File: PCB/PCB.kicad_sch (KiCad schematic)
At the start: 21 parts, among them J1 Conn_01x06_Female, U13 74HC165, U16 74HC165

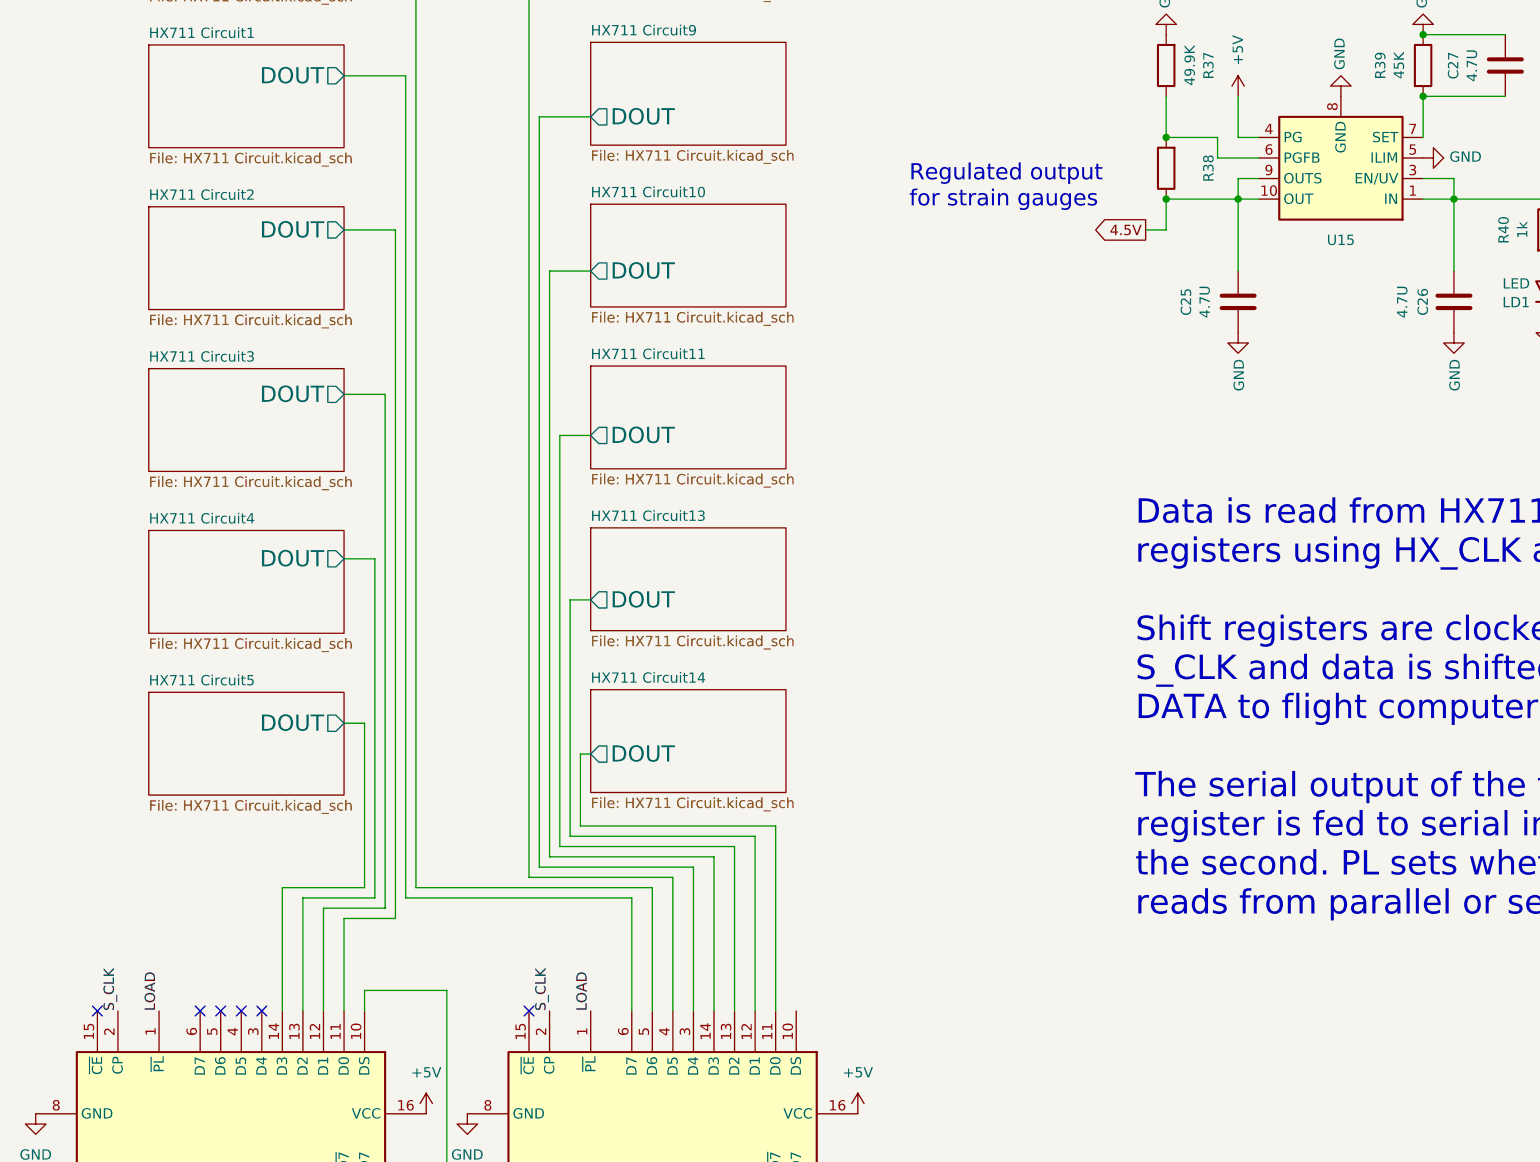
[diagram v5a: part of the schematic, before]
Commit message: Add second decoupling cap to HXs
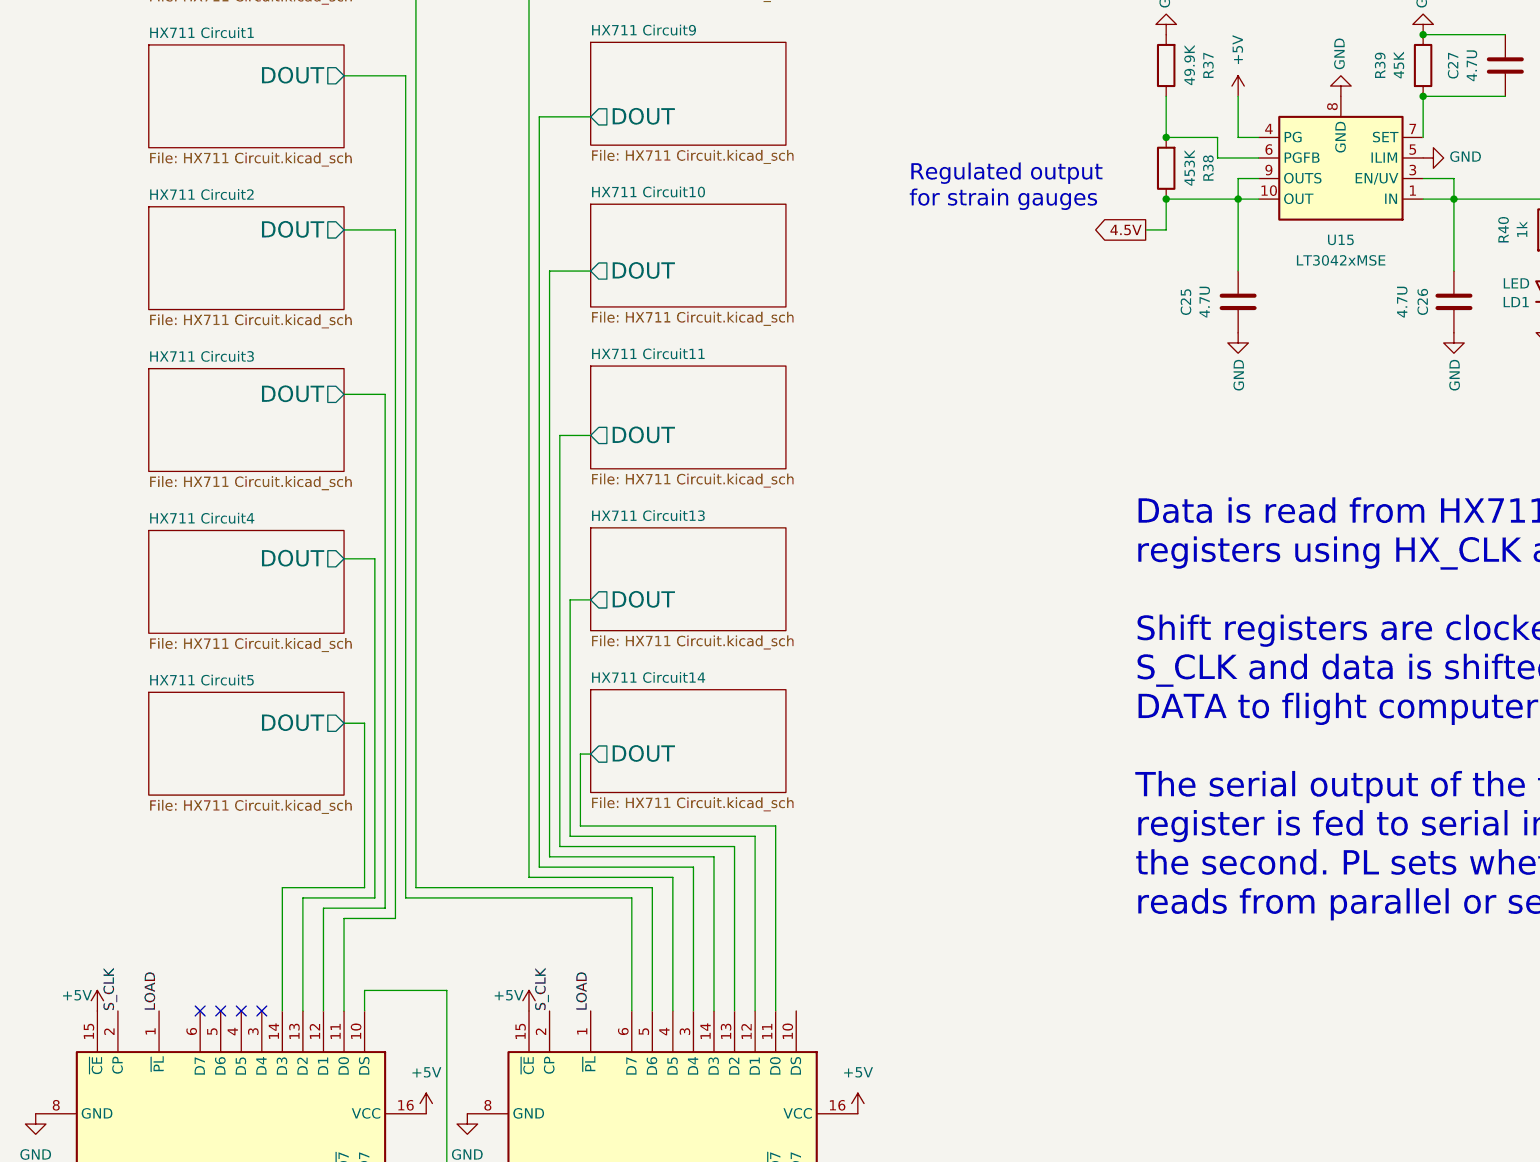
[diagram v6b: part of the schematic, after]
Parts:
- R38: value (none) -> 453K; footprint (none) -> Resistor_SMD:R_0805_2012Metric_Pad1.20x1.40mm_HandSolder
- U15: value (none) -> LT3042xMSE; footprint (none) -> Package_SO:MSOP-10-1EP_3x3mm_P0.5mm_EP1.68x1.88mm
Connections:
- net +5V: now also U13.15 (~{CE}), U16.15 (~{CE})
- no-connect marks 8 -> 6
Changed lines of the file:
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@@
   (no_connect (at 45.72 165.1))
   (no_connect (at 40.64 165.1))
-  (no_connect (at 81.28 165.1))
   (no_connect (at 58.42 190.5))
   (no_connect (at 111.76 190.5))
   (no_connect (at 48.26 165.1))
-  (no_connect (at 27.94 165.1))
   (no_connect (at 43.18 165.1))
   (wire (pts (xy 64.77 68.58) (xy 64.77 153.67))
@@
     (in_bom yes) (on_board yes)
     (property "Reference" "R38" (id 0) (at 165.2778 60.96 90))
-    (property "Value" "" (id 1) (at 162.9664 60.96 90))
-    (property "Footprint" "" (id 2) (at 161.798 60.96 90)
+    (property "Value" "453K" (id 1) (at 162.9664 60.96 90))
+    (property "Footprint" "Resistor_SMD:R_0805_2012Metric_Pad1.20x1.40mm_HandSolder" (id 2) (at 161.798 60.96 90)
       (effects (font (size 1.27 1.27)) hide)
     )
@@
     (in_bom yes) (on_board yes) (fields_autoplaced)
     (property "Reference" "U15" (id 0) (at 181.61 69.85 0))
-    (property "Value" "" (id 1) (at 181.61 72.39 0))
-    (property "Footprint" "" (id 2) (at 181.61 70.485 0)
+    (property "Value" "LT3042xMSE" (id 1) (at 181.61 72.39 0))
+    (property "Footprint" "Package_SO:MSOP-10-1EP_3x3mm_P0.5mm_EP1.68x1.88mm" (id 2) (at 181.61 70.485 0)
       (effects (font (size 1.27 1.27)) hide)
     )
@@
     )
   )
+  (symbol (lib_id "power:+5V") (at 27.94 165.1 0) (unit 1)
+    (in_bom yes) (on_board yes)
+    (property "Reference" "#PWR?" (id 0) (at 27.94 168.91 0)
+      (effects (font (size 1.27 1.27)) hide)
+    )
+    (property "Value" "+5V" (id 1) (at 25.4 163.195 0))
+    (property "Footprint" "" (id 2) (at 27.94 165.1 0)
+      (effects (font (size 1.27 1.27)) hide)
+    )
+    (property "Datasheet" "" (id 3) (at 27.94 165.1 0)
+      (effects (font (size 1.27 1.27)) hide)
+    )
+    (pin "1")
+  )
   (symbol (lib_id "Mechanical:MountingHole") (at 255.27 73.66 180) (unit 1)
     (in_bom yes) (on_board yes)
@@
       (effects (font (size 1.27 1.27)) hide)
     )
+  )
+  (symbol (lib_id "power:+5V") (at 81.28 165.1 0) (unit 1)
+    (in_bom yes) (on_board yes)
+    (property "Reference" "#PWR?" (id 0) (at 81.28 168.91 0)
+      (effects (font (size 1.27 1.27)) hide)
+    )
+    (property "Value" "+5V" (id 1) (at 78.74 163.195 0))
+    (property "Footprint" "" (id 2) (at 81.28 165.1 0)
+      (effects (font (size 1.27 1.27)) hide)
+    )
+    (property "Datasheet" "" (id 3) (at 81.28 165.1 0)
+      (effects (font (size 1.27 1.27)) hide)
+    )
+    (pin "1")
   )
   (symbol (lib_id "74xx:74HC165") (at 99.06 177.8 270) (unit 1)
@@
       (reference "#PWR0176") (unit 1) (value "GND") (footprint "")
     )
+    (path "/73cb09ad-e380-49f3-bc9d-038b1104bc93"
+      (reference "#PWR?") (unit 1) (value "+5V") (footprint "")
+    )
+    (path "/ad4b4db0-56fe-4cd1-a5ce-265d1900b152"
+      (reference "#PWR?") (unit 1) (value "+5V") (footprint "")
+    )
     (path "/865df6f9-fa66-4b43-929e-1913f975c2d0/111274e0-7b7d-4557-ab89-a261603ab22a"
       (reference "C1") (unit 1) (value "10U") (footprint "Capacitor_SMD:C_0805_2012Metric_Pad1.18x1.45mm_HandSolder")
@@
       (reference "C27") (unit 1) (value "4.7U") (footprint "Capacitor_SMD:C_0805_2012Metric_Pad1.18x1.45mm_HandSolder")
     )
+    (path "/865df6f9-fa66-4b43-929e-1913f975c2d0/2da591a3-6e1f-401e-b546-57e02f378ea9"
+      (reference "C28") (unit 1) (value "C") (footprint "")
+    )
+    (path "/0821f14b-d29c-4d59-b007-c0ebd9554832/2da591a3-6e1f-401e-b546-57e02f378ea9"
+      (reference "C29") (unit 1) (value "C") (footprint "")
+    )
+    (path "/348f29cd-068e-4363-9c21-09b34e523a46/2da591a3-6e1f-401e-b546-57e02f378ea9"
+      (reference "C30") (unit 1) (value "C") (footprint "")
+    )
+    (path "/eababe2a-0ecd-4427-a6f7-2ec75821d4fc/2da591a3-6e1f-401e-b546-57e02f378ea9"
+      (reference "C31") (unit 1) (value "C") (footprint "")
+    )
+    (path "/55c2d934-244c-44fa-a407-b54a366ca226/2da591a3-6e1f-401e-b546-57e02f378ea9"
+      (reference "C32") (unit 1) (value "C") (footprint "")
+    )
+    (path "/7ce80e6b-d043-4f1b-ad6b-3c069ab9b9d7/2da591a3-6e1f-401e-b546-57e02f378ea9"
+      (reference "C33") (unit 1) (value "C") (footprint "")
+    )
+    (path "/08e9dfb0-f6cf-445e-a76d-3f029063dc7e/2da591a3-6e1f-401e-b546-57e02f378ea9"
+      (reference "C34") (unit 1) (value "C") (footprint "")
+    )
+    (path "/fb1b1fbb-996e-4607-8c6e-29ed755bddb1/2da591a3-6e1f-401e-b546-57e02f378ea9"
+      (reference "C35") (unit 1) (value "C") (footprint "")
+    )
+    (path "/c3166b72-45ca-4bb3-84d0-d9a7dc830ff6/2da591a3-6e1f-401e-b546-57e02f378ea9"
+      (reference "C36") (unit 1) (value "C") (footprint "")
+    )
+    (path "/570e1fbc-5905-405a-9db3-c7c35f19abe3/2da591a3-6e1f-401e-b546-57e02f378ea9"
+      (reference "C37") (unit 1) (value "C") (footprint "")
+    )
+    (path "/437b6eb2-c2ed-4592-b41e-b7f1e7300163/2da591a3-6e1f-401e-b546-57e02f378ea9"
+      (reference "C38") (unit 1) (value "C") (footprint "")
+    )
+    (path "/6eed81f2-9ea8-4b15-9b25-b30a760a9be7/2da591a3-6e1f-401e-b546-57e02f378ea9"
+      (reference "C39") (unit 1) (value "C") (footprint "")
+    )
     (path "/74da8817-111b-471e-90b9-b326ffd8df1d"

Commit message: Finish trace routing
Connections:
- no-connect marks 6 -> 7
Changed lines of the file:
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@@
   )
   (no_connect (at 45.72 165.1))
+  (no_connect (at 114.3 165.1))
   (no_connect (at 40.64 165.1))
   (no_connect (at 58.42 190.5))
@@
   (symbol (lib_id "power:+5V") (at 27.94 165.1 0) (unit 1)
     (in_bom yes) (on_board yes)
-    (property "Reference" "#PWR?" (id 0) (at 27.94 168.91 0)
+    (property "Reference" "#PWR0178" (id 0) (at 27.94 168.91 0)
       (effects (font (size 1.27 1.27)) hide)
     )
@@
   (symbol (lib_id "power:+5V") (at 81.28 165.1 0) (unit 1)
     (in_bom yes) (on_board yes)
-    (property "Reference" "#PWR?" (id 0) (at 81.28 168.91 0)
+    (property "Reference" "#PWR0177" (id 0) (at 81.28 168.91 0)
       (effects (font (size 1.27 1.27)) hide)
     )
@@
       (reference "#PWR0176") (unit 1) (value "GND") (footprint "")
     )
+    (path "/ad4b4db0-56fe-4cd1-a5ce-265d1900b152"
+      (reference "#PWR0177") (unit 1) (value "+5V") (footprint "")
+    )
     (path "/73cb09ad-e380-49f3-bc9d-038b1104bc93"
-      (reference "#PWR?") (unit 1) (value "+5V") (footprint "")
-    )
-    (path "/ad4b4db0-56fe-4cd1-a5ce-265d1900b152"
-      (reference "#PWR?") (unit 1) (value "+5V") (footprint "")
+      (reference "#PWR0178") (unit 1) (value "+5V") (footprint "")
     )
     (path "/865df6f9-fa66-4b43-929e-1913f975c2d0/111274e0-7b7d-4557-ab89-a261603ab22a"
@@
     )
     (path "/865df6f9-fa66-4b43-929e-1913f975c2d0/e3b7f339-eb91-410f-8a0a-b3d110988d30"
-      (reference "C2") (unit 1) (value "0.01U") (footprint "Capacitor_SMD:C_0805_2012Metric_Pad1.18x1.45mm_HandSolder")
+      (reference "C2") (unit 1) (value "U01") (footprint "Capacitor_SMD:C_0805_2012Metric_Pad1.18x1.45mm_HandSolder")
     )
     (path "/0821f14b-d29c-4d59-b007-c0ebd9554832/111274e0-7b7d-4557-ab89-a261603ab22a"
@@
     )
     (path "/0821f14b-d29c-4d59-b007-c0ebd9554832/e3b7f339-eb91-410f-8a0a-b3d110988d30"
-      (reference "C4") (unit 1) (value "0.01U") (footprint "Capacitor_SMD:C_0805_2012Metric_Pad1.18x1.45mm_HandSolder")
+      (reference "C4") (unit 1) (value "U01") (footprint "Capacitor_SMD:C_0805_2012Metric_Pad1.18x1.45mm_HandSolder")
     )
     (path "/348f29cd-068e-4363-9c21-09b34e523a46/111274e0-7b7d-4557-ab89-a261603ab22a"
@@
     )
     (path "/348f29cd-068e-4363-9c21-09b34e523a46/e3b7f339-eb91-410f-8a0a-b3d110988d30"
-      (reference "C6") (unit 1) (value "0.01U") (footprint "Capacitor_SMD:C_0805_2012Metric_Pad1.18x1.45mm_HandSolder")
+      (reference "C6") (unit 1) (value "U01") (footprint "Capacitor_SMD:C_0805_2012Metric_Pad1.18x1.45mm_HandSolder")
     )
     (path "/eababe2a-0ecd-4427-a6f7-2ec75821d4fc/111274e0-7b7d-4557-ab89-a261603ab22a"
@@
     )
     (path "/eababe2a-0ecd-4427-a6f7-2ec75821d4fc/e3b7f339-eb91-410f-8a0a-b3d110988d30"
-      (reference "C8") (unit 1) (value "0.01U") (footprint "Capacitor_SMD:C_0805_2012Metric_Pad1.18x1.45mm_HandSolder")
+      (reference "C8") (unit 1) (value "U01") (footprint "Capacitor_SMD:C_0805_2012Metric_Pad1.18x1.45mm_HandSolder")
     )
     (path "/55c2d934-244c-44fa-a407-b54a366ca226/111274e0-7b7d-4557-ab89-a261603ab22a"
@@
     )
     (path "/55c2d934-244c-44fa-a407-b54a366ca226/e3b7f339-eb91-410f-8a0a-b3d110988d30"
-      (reference "C10") (unit 1) (value "0.01U") (footprint "Capacitor_SMD:C_0805_2012Metric_Pad1.18x1.45mm_HandSolder")
+      (reference "C10") (unit 1) (value "U01") (footprint "Capacitor_SMD:C_0805_2012Metric_Pad1.18x1.45mm_HandSolder")
     )
     (path "/7ce80e6b-d043-4f1b-ad6b-3c069ab9b9d7/111274e0-7b7d-4557-ab89-a261603ab22a"
@@
     )
     (path "/7ce80e6b-d043-4f1b-ad6b-3c069ab9b9d7/e3b7f339-eb91-410f-8a0a-b3d110988d30"
-      (reference "C12") (unit 1) (value "0.01U") (footprint "Capacitor_SMD:C_0805_2012Metric_Pad1.18x1.45mm_HandSolder")
+      (reference "C12") (unit 1) (value "U01") (footprint "Capacitor_SMD:C_0805_2012Metric_Pad1.18x1.45mm_HandSolder")
     )
     (path "/08e9dfb0-f6cf-445e-a76d-3f029063dc7e/111274e0-7b7d-4557-ab89-a261603ab22a"
@@
     )
     (path "/08e9dfb0-f6cf-445e-a76d-3f029063dc7e/e3b7f339-eb91-410f-8a0a-b3d110988d30"
-      (reference "C14") (unit 1) (value "0.01U") (footprint "Capacitor_SMD:C_0805_2012Metric_Pad1.18x1.45mm_HandSolder")
+      (reference "C14") (unit 1) (value "U01") (footprint "Capacitor_SMD:C_0805_2012Metric_Pad1.18x1.45mm_HandSolder")
     )
     (path "/fb1b1fbb-996e-4607-8c6e-29ed755bddb1/111274e0-7b7d-4557-ab89-a261603ab22a"
@@
     )
     (path "/fb1b1fbb-996e-4607-8c6e-29ed755bddb1/e3b7f339-eb91-410f-8a0a-b3d110988d30"
-      (reference "C16") (unit 1) (value "0.01U") (footprint "Capacitor_SMD:C_0805_2012Metric_Pad1.18x1.45mm_HandSolder")
+      (reference "C16") (unit 1) (value "U01") (footprint "Capacitor_SMD:C_0805_2012Metric_Pad1.18x1.45mm_HandSolder")
     )
     (path "/c3166b72-45ca-4bb3-84d0-d9a7dc830ff6/111274e0-7b7d-4557-ab89-a261603ab22a"
@@
     )
     (path "/c3166b72-45ca-4bb3-84d0-d9a7dc830ff6/e3b7f339-eb91-410f-8a0a-b3d110988d30"
-      (reference "C18") (unit 1) (value "0.01U") (footprint "Capacitor_SMD:C_0805_2012Metric_Pad1.18x1.45mm_HandSolder")
+      (reference "C18") (unit 1) (value "U01") (footprint "Capacitor_SMD:C_0805_2012Metric_Pad1.18x1.45mm_HandSolder")
     )
     (path "/570e1fbc-5905-405a-9db3-c7c35f19abe3/111274e0-7b7d-4557-ab89-a261603ab22a"
@@
     )
     (path "/570e1fbc-5905-405a-9db3-c7c35f19abe3/e3b7f339-eb91-410f-8a0a-b3d110988d30"
-      (reference "C20") (unit 1) (value "0.01U") (footprint "Capacitor_SMD:C_0805_2012Metric_Pad1.18x1.45mm_HandSolder")
+      (reference "C20") (unit 1) (value "U01") (footprint "Capacitor_SMD:C_0805_2012Metric_Pad1.18x1.45mm_HandSolder")
     )
     (path "/437b6eb2-c2ed-4592-b41e-b7f1e7300163/111274e0-7b7d-4557-ab89-a261603ab22a"
@@
     )
     (path "/437b6eb2-c2ed-4592-b41e-b7f1e7300163/e3b7f339-eb91-410f-8a0a-b3d110988d30"
-      (reference "C22") (unit 1) (value "0.01U") (footprint "Capacitor_SMD:C_0805_2012Metric_Pad1.18x1.45mm_HandSolder")
+      (reference "C22") (unit 1) (value "U01") (footprint "Capacitor_SMD:C_0805_2012Metric_Pad1.18x1.45mm_HandSolder")
     )
     (path "/6eed81f2-9ea8-4b15-9b25-b30a760a9be7/111274e0-7b7d-4557-ab89-a261603ab22a"
@@
     )
     (path "/6eed81f2-9ea8-4b15-9b25-b30a760a9be7/e3b7f339-eb91-410f-8a0a-b3d110988d30"
-      (reference "C24") (unit 1) (value "0.01U") (footprint "Capacitor_SMD:C_0805_2012Metric_Pad1.18x1.45mm_HandSolder")
+      (reference "C24") (unit 1) (value "U01") (footprint "Capacitor_SMD:C_0805_2012Metric_Pad1.18x1.45mm_HandSolder")
     )
     (path "/00000000-0000-0000-0000-00006110ef58"
@@
     )
     (path "/865df6f9-fa66-4b43-929e-1913f975c2d0/2da591a3-6e1f-401e-b546-57e02f378ea9"
-      (reference "C28") (unit 1) (value "C") (footprint "")
+      (reference "C28") (unit 1) (value "U01") (footprint "Capacitor_SMD:C_0805_2012Metric_Pad1.18x1.45mm_HandSolder")
     )
     (path "/0821f14b-d29c-4d59-b007-c0ebd9554832/2da591a3-6e1f-401e-b546-57e02f378ea9"
-      (reference "C29") (unit 1) (value "C") (footprint "")
+      (reference "C29") (unit 1) (value "U01") (footprint "Capacitor_SMD:C_0805_2012Metric_Pad1.18x1.45mm_HandSolder")
     )
     (path "/348f29cd-068e-4363-9c21-09b34e523a46/2da591a3-6e1f-401e-b546-57e02f378ea9"
-      (reference "C30") (unit 1) (value "C") (footprint "")
+      (reference "C30") (unit 1) (value "U01") (footprint "Capacitor_SMD:C_0805_2012Metric_Pad1.18x1.45mm_HandSolder")
     )
     (path "/eababe2a-0ecd-4427-a6f7-2ec75821d4fc/2da591a3-6e1f-401e-b546-57e02f378ea9"
-      (reference "C31") (unit 1) (value "C") (footprint "")
+      (reference "C31") (unit 1) (value "U01") (footprint "Capacitor_SMD:C_0805_2012Metric_Pad1.18x1.45mm_HandSolder")
     )
     (path "/55c2d934-244c-44fa-a407-b54a366ca226/2da591a3-6e1f-401e-b546-57e02f378ea9"
-      (reference "C32") (unit 1) (value "C") (footprint "")
+      (reference "C32") (unit 1) (value "U01") (footprint "Capacitor_SMD:C_0805_2012Metric_Pad1.18x1.45mm_HandSolder")
     )
     (path "/7ce80e6b-d043-4f1b-ad6b-3c069ab9b9d7/2da591a3-6e1f-401e-b546-57e02f378ea9"
-      (reference "C33") (unit 1) (value "C") (footprint "")
+      (reference "C33") (unit 1) (value "U01") (footprint "Capacitor_SMD:C_0805_2012Metric_Pad1.18x1.45mm_HandSolder")
     )
     (path "/08e9dfb0-f6cf-445e-a76d-3f029063dc7e/2da591a3-6e1f-401e-b546-57e02f378ea9"
-      (reference "C34") (unit 1) (value "C") (footprint "")
+      (reference "C34") (unit 1) (value "U01") (footprint "Capacitor_SMD:C_0805_2012Metric_Pad1.18x1.45mm_HandSolder")
     )
     (path "/fb1b1fbb-996e-4607-8c6e-29ed755bddb1/2da591a3-6e1f-401e-b546-57e02f378ea9"
-      (reference "C35") (unit 1) (value "C") (footprint "")
+      (reference "C35") (unit 1) (value "U01") (footprint "Capacitor_SMD:C_0805_2012Metric_Pad1.18x1.45mm_HandSolder")
     )
     (path "/c3166b72-45ca-4bb3-84d0-d9a7dc830ff6/2da591a3-6e1f-401e-b546-57e02f378ea9"
-      (reference "C36") (unit 1) (value "C") (footprint "")
+      (reference "C36") (unit 1) (value "U01") (footprint "Capacitor_SMD:C_0805_2012Metric_Pad1.18x1.45mm_HandSolder")
     )
     (path "/570e1fbc-5905-405a-9db3-c7c35f19abe3/2da591a3-6e1f-401e-b546-57e02f378ea9"
-      (reference "C37") (unit 1) (value "C") (footprint "")
+      (reference "C37") (unit 1) (value "U01") (footprint "Capacitor_SMD:C_0805_2012Metric_Pad1.18x1.45mm_HandSolder")
     )
     (path "/437b6eb2-c2ed-4592-b41e-b7f1e7300163/2da591a3-6e1f-401e-b546-57e02f378ea9"
-      (reference "C38") (unit 1) (value "C") (footprint "")
+      (reference "C38") (unit 1) (value "U01") (footprint "Capacitor_SMD:C_0805_2012Metric_Pad1.18x1.45mm_HandSolder")
     )
     (path "/6eed81f2-9ea8-4b15-9b25-b30a760a9be7/2da591a3-6e1f-401e-b546-57e02f378ea9"
-      (reference "C39") (unit 1) (value "C") (footprint "")
+      (reference "C39") (unit 1) (value "U01") (footprint "Capacitor_SMD:C_0805_2012Metric_Pad1.18x1.45mm_HandSolder")
     )
     (path "/74da8817-111b-471e-90b9-b326ffd8df1d"
